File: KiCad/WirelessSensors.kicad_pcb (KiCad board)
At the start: 2 copper layers, 60.5 x 51 mm, 45 parts, among them IC1 ATMEGA328-P, P1 PWR +, P11 PULSE, P12 PULSE 2, P13 NRF24, P2 PWR JMP, P4 D24V3F3, P6 External, Q1 BC547, Q2 FQP27P06 (PFET)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

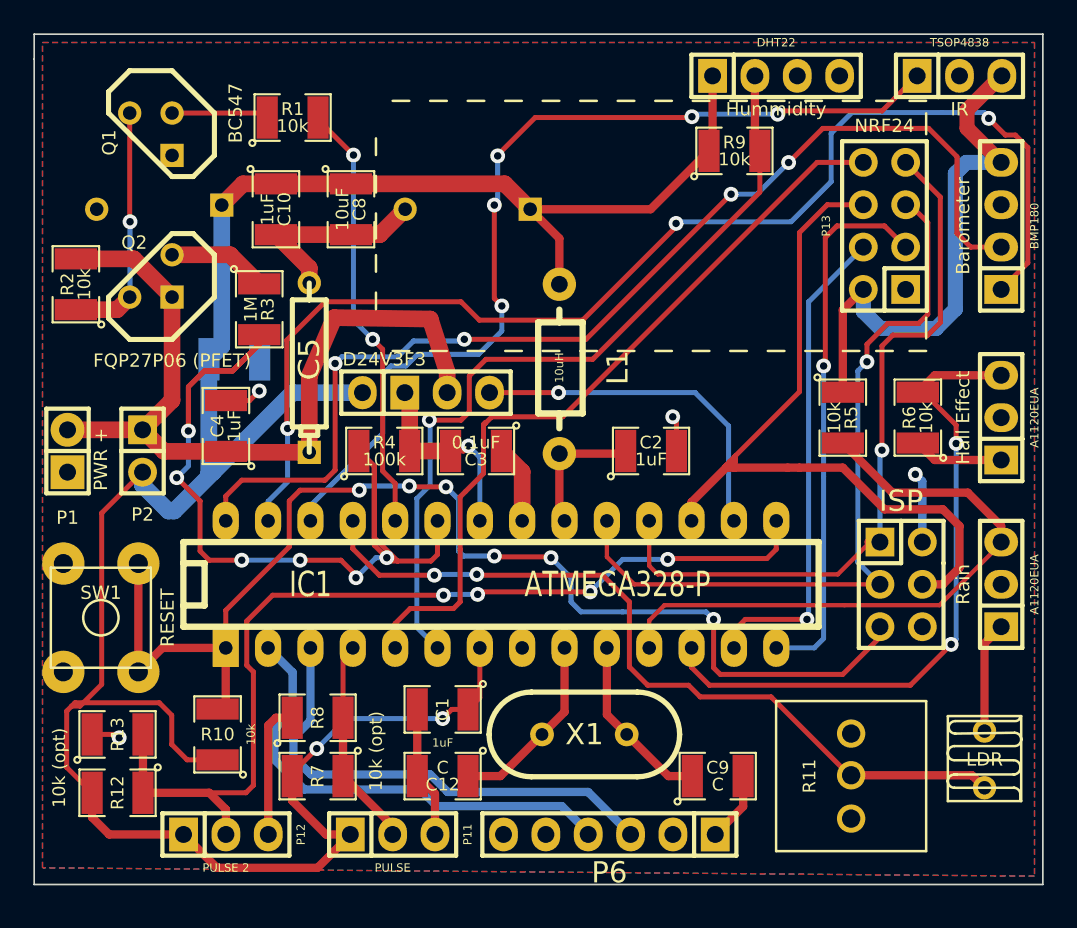
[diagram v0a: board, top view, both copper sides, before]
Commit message: New mounting holes in pcb layout
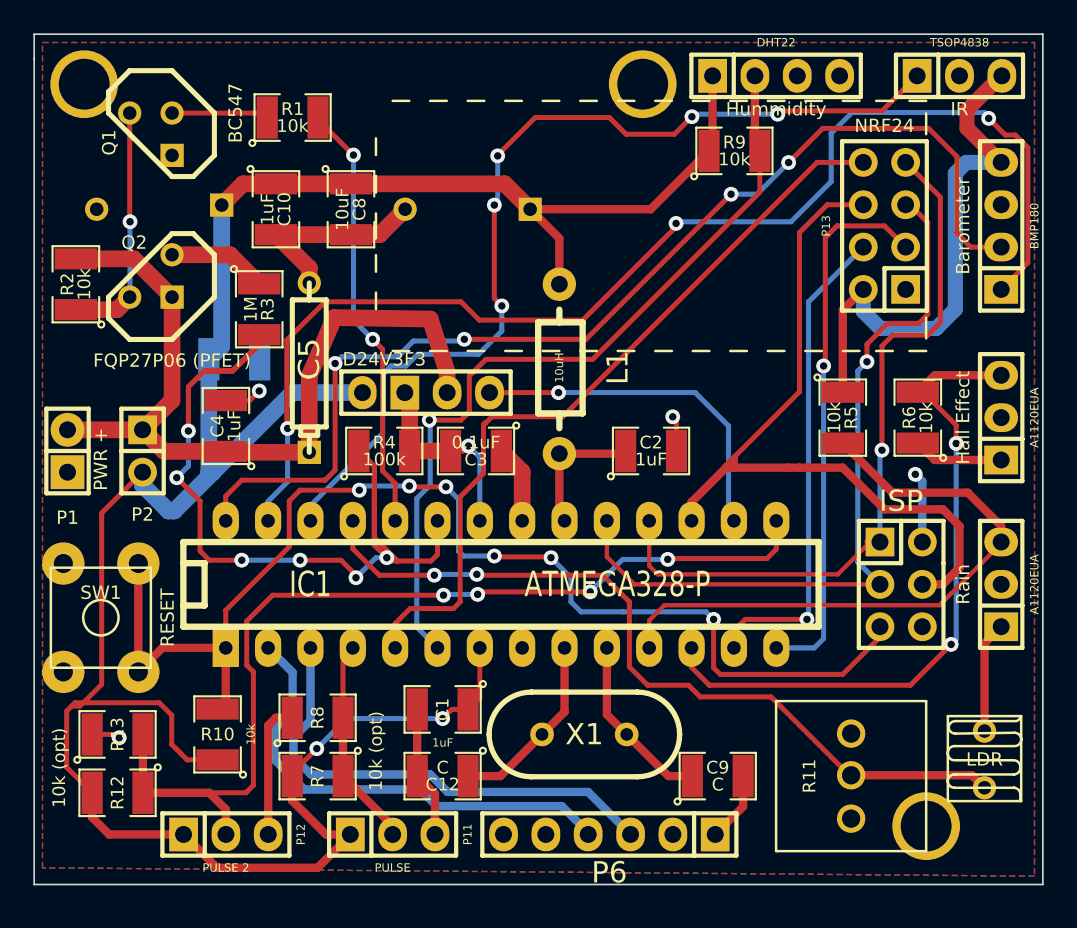
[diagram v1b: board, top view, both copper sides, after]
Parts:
- added Mount: P***, Connect:1pin, F.Cu at (124.0, 48.0)
- added Mount: P***, Connect:1pin, F.Cu at (157.5, 48.0)
- added Mount: P***, Connect:1pin, F.Cu at (174.5, 92.5)
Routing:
- net ADC3: track 56.8 -> 57.6 mm

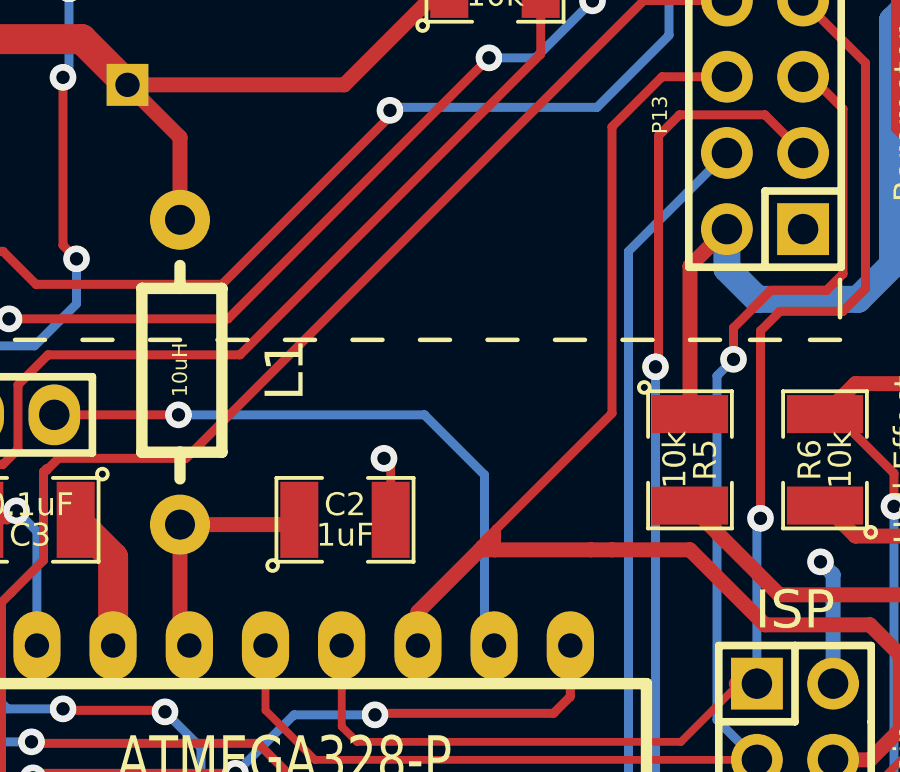
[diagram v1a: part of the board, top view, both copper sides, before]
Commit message: added additional details to PCB design
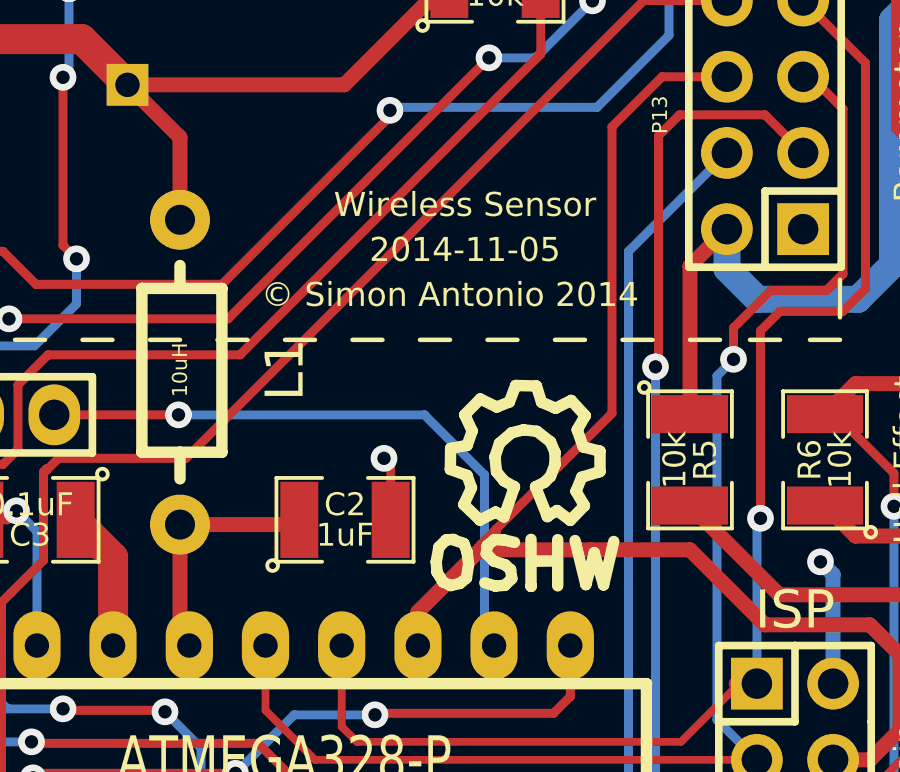
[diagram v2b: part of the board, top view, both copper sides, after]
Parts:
- added ?: , Symbols:Symbol_OSHW-Logo_SilkScreen, F.Cu at (164.0, 68.0)
- added Sym: Symbol_OSHW-Logo_SilkScreen_BIG_07Jul2012, Symbols:Symbol_OSHW-Logo_SilkScreen_BIG, B.Cu at (161.5, 43.0)
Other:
- board text added: "2014-11-05"
- board text added: "Wireless Sensor"
- board text added: "Wireless Sensor © Simon Antonio 2014"
- board text added: "© Simon Antonio 2014"
